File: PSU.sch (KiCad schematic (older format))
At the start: 8 parts

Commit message: created pcb
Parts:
- R5: renamed from R?; footprint Main_LIB:R_0603 -> MAIN_PCB_LIB:R_0603
- gave numbers to parts that had none: 7
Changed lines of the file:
@@
 $Descr A4 11693 8268
 encoding utf-8
-Sheet 2 4
+Sheet 2 5
 Title ""
 Date ""
@@
 	4400 2600 4550 2600
 $Comp
-L Main_Library:C_100nF_0603_50V C?
+L Main_Library:C_100nF_0603_50V C1
 U 1 1 6152505F
 P 3550 2750
-F 0 "C?" H 3628 2796 50  0000 L CNN
+F 0 "C1" H 3628 2796 50  0000 L CNN
 F 1 "C_100nF_0603_50V" H 3500 3100 50  0001 C CNN
 F 2 "MAIN_PCB_LIB:C_0603" H 3500 3100 50  0001 C CNN
@@
 	3550 2600 3800 2600
 $Comp
-L Main_Library:GND #GND?
+L Main_Library:GND #GND04
 U 1 1 61525852
 P 3550 2900
-F 0 "#GND?" H 3390 2880 50  0001 C CNN
+F 0 "#GND04" H 3390 2880 50  0001 C CNN
 F 1 "GND" H 3390 2880 50  0001 C CNN
 F 2 "" H 3460 2840 50  0001 C CNN
@@
 $EndComp
 $Comp
-L Main_Library:R_3K_0603 R?
+L Main_Library:R_3K_0603 R3
 U 1 1 61527697
 P 4550 2800
-F 0 "R?" H 4603 2846 50  0000 L CNN
+F 0 "R3" H 4603 2846 50  0000 L CNN
 F 1 "R_3K_0603" H 4550 2800 50  0001 C CNN
 F 2 "MAIN_PCB_LIB:R_0603" H 4550 2800 50  0001 C CNN
@@
 	4100 3000 4550 3000
 $Comp
-L Main_Library:GND #GND?
+L Main_Library:GND #GND06
 U 1 1 6152B9B3
 P 4250 3200
-F 0 "#GND?" H 4090 3180 50  0001 C CNN
+F 0 "#GND06" H 4090 3180 50  0001 C CNN
 F 1 "GND" H 4090 3180 50  0001 C CNN
 F 2 "" H 4160 3140 50  0001 C CNN
@@
 	4200 3200 4250 3200
 $Comp
-L Main_Library:U_LM317_TH U?
+L Main_Library:U_LM317_TH U1
 U 1 1 61586E8A
 P 4100 2600
-F 0 "U?" H 4100 2775 50  0000 C CNN
+F 0 "U1" H 4100 2775 50  0000 C CNN
 F 1 "U_LM317_TH" H 4100 3000 50  0001 C CNN
 F 2 "MAIN_PCB_LIB:U_LM317_TI_TH" H 4100 3000 50  0001 C CNN
@@
 $EndComp
 $Comp
-L Main_Library:R_10K_Potmeter R?
+L Main_Library:R_10K_Potmeter R2
 U 1 1 615893FF
 P 4100 3200
-F 0 "R?" H 4047 3246 50  0000 R CNN
+F 0 "R2" H 4047 3246 50  0000 R CNN
 F 1 "R_10K_Potmeter" H 4200 3500 50  0001 C CNN
 F 2 "MAIN_PCB_LIB:R_TH_POT_P160series" H 4200 3500 50  0001 C CNN
@@
 	3100 3800 3600 3800
 $Comp
-L Main_Library:C_100nF_0603_50V C?
+L Main_Library:C_100nF_0603_50V C2
 U 1 1 61594EF5
 P 3600 3950
-F 0 "C?" H 3678 3996 50  0000 L CNN
+F 0 "C2" H 3678 3996 50  0000 L CNN
 F 1 "C_100nF_0603_50V" H 3550 4300 50  0001 C CNN
 F 2 "MAIN_PCB_LIB:C_0603" H 3550 4300 50  0001 C CNN
@@
 	3600 3800 3850 3800
 $Comp
-L Main_Library:GND #GND?
+L Main_Library:GND #GND05
 U 1 1 61594EFD
 P 3600 4100
-F 0 "#GND?" H 3440 4080 50  0001 C CNN
+F 0 "#GND05" H 3440 4080 50  0001 C CNN
 F 1 "GND" H 3440 4080 50  0001 C CNN
 F 2 "" H 3510 4040 50  0001 C CNN
@@
 $EndComp
 $Comp
-L Main_Library:R_3K_0603 R?
+L Main_Library:R_3K_0603 R4
 U 1 1 61594F05
 P 4600 4000
-F 0 "R?" H 4653 4046 50  0000 L CNN
+F 0 "R4" H 4653 4046 50  0000 L CNN
 F 1 "R_3K_0603" H 4600 4000 50  0001 C CNN
 F 2 "MAIN_PCB_LIB:R_0603" H 4600 4000 50  0001 C CNN
@@
 	4150 4200 4600 4200
 $Comp
-L Main_Library:U_LM317_TH U?
+L Main_Library:U_LM317_TH U2
 U 1 1 61594F17
 P 4150 3800
-F 0 "U?" H 4150 3975 50  0000 C CNN
+F 0 "U2" H 4150 3975 50  0000 C CNN
 F 1 "U_LM317_TH" H 4150 4200 50  0001 C CNN
 F 2 "MAIN_PCB_LIB:U_LM317_TI_TH" H 4150 4200 50  0001 C CNN
@@
 5V
 $Comp
-L Main_Library:R_9K1_0603 R?
+L Main_Library:R_9K1_0603 R5
 U 1 1 615992A6
 P 4600 4350
-F 0 "R?" H 4653 4388 39  0000 L CNN
+F 0 "R5" H 4653 4388 39  0000 L CNN
 F 1 "R_9K1_0603" H 4550 4900 39  0001 C CNN
-F 2 "Main_LIB:R_0603" H 4600 4850 39  0001 C CNN
+F 2 "MAIN_PCB_LIB:R_0603" H 4600 4850 39  0001 C CNN
 F 3 "" H 4550 4500 39  0001 C CNN
 F 4 "9K1" H 4653 4313 39  0000 L CNN "Waarde"
@@
 Connection ~ 4600 4200
 $Comp
-L Main_Library:GND #GND?
+L Main_Library:GND #GND07
 U 1 1 61599DC1
 P 4600 4500
-F 0 "#GND?" H 4440 4480 50  0001 C CNN
+F 0 "#GND07" H 4440 4480 50  0001 C CNN
 F 1 "GND" H 4440 4480 50  0001 C CNN
 F 2 "" H 4510 4440 50  0001 C CNN

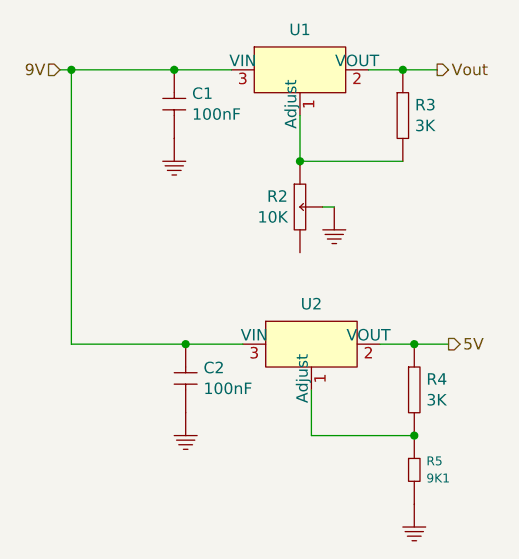
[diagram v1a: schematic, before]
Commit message: added raspberry pi hat pcb outline and layout
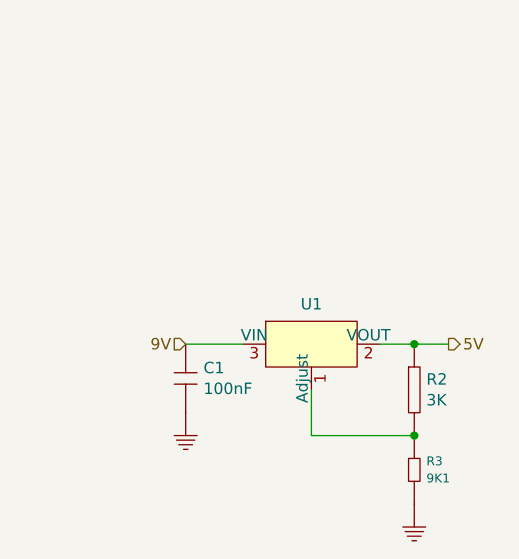
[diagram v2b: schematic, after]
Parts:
- removed C1: C_100nF_0603_50V, MAIN_PCB_LIB:C_0603, symbol Main_Library:C_100nF_0603_50V
- removed R2: R_10K_Potmeter, MAIN_PCB_LIB:R_TH_POT_P160series, symbol Main_Library:R_10K_Potmeter
- removed R3: R_3K_0603, MAIN_PCB_LIB:R_0603, symbol Main_Library:R_3K_0603
- removed U1: U_LM317_TH, MAIN_PCB_LIB:U_LM317_TI_TH, symbol Main_Library:U_LM317_TH
- renumbered C2 to C1, R4 to R2, R5 to R3, U2 to U1
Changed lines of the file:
@@
 Comment4 ""
 $EndDescr
-Text HLabel 3050 2600 0    50   Input ~ 0
+Text HLabel 3600 3800 0    50   Input ~ 0
 9V
-Text HLabel 4700 2600 2    50   Output ~ 0
-Vout
 Wire Wire Line
-	4400 2600 4550 2600
+	4450 3800 4600 3800
 $Comp
 L Main_Library:C_100nF_0603_50V C1
-U 1 1 6152505F
-P 3550 2750
-F 0 "C1" H 3628 2796 50  0000 L CNN
-F 1 "C_100nF_0603_50V" H 3500 3100 50  0001 C CNN
-F 2 "MAIN_PCB_LIB:C_0603" H 3500 3100 50  0001 C CNN
-F 3 "" H 3550 2950 50  0001 C CNN
-F 4 "C105174" H 3500 3050 50  0001 C CNN "LCSC"
-F 5 "100nF" H 3628 2705 50  0000 L CNN "Waarde"
-	1    3550 2750
-	1    0    0    -1
-$EndComp
-Connection ~ 3550 2600
-Wire Wire Line
-	3550 2600 3800 2600
-$Comp
-L Main_Library:GND #GND04
-U 1 1 61525852
-P 3550 2900
-F 0 "#GND04" H 3390 2880 50  0001 C CNN
-F 1 "GND" H 3390 2880 50  0001 C CNN
-F 2 "" H 3460 2840 50  0001 C CNN
-F 3 "" H 3460 2840 50  0001 C CNN
-	1    3550 2900
-	1    0    0    -1
-$EndComp
-$Comp
-L Main_Library:R_3K_0603 R3
-U 1 1 61527697
-P 4550 2800
-F 0 "R3" H 4603 2846 50  0000 L CNN
-F 1 "R_3K_0603" H 4550 2800 50  0001 C CNN
-F 2 "MAIN_PCB_LIB:R_0603" H 4550 2800 50  0001 C CNN
-F 3 "" H 4550 2800 50  0001 C CNN
-F 4 "603-RC0603FR-7W3KL" H 4550 2800 50  0001 C CNN "mouser"
-F 5 "3K" H 4603 2755 50  0000 L CNN "waarde"
-	1    4550 2800
-	1    0    0    -1
-$EndComp
-Connection ~ 4550 2600
-Wire Wire Line
-	4550 2600 4700 2600
-Wire Wire Line
-	4100 3000 4100 2800
-Wire Wire Line
-	4100 3000 4550 3000
-$Comp
-L Main_Library:GND #GND06
-U 1 1 6152B9B3
-P 4250 3200
-F 0 "#GND06" H 4090 3180 50  0001 C CNN
-F 1 "GND" H 4090 3180 50  0001 C CNN
-F 2 "" H 4160 3140 50  0001 C CNN
-F 3 "" H 4160 3140 50  0001 C CNN
-	1    4250 3200
-	1    0    0    -1
-$EndComp
-Wire Wire Line
-	4200 3200 4250 3200
-$Comp
-L Main_Library:U_LM317_TH U1
-U 1 1 61586E8A
-P 4100 2600
-F 0 "U1" H 4100 2775 50  0000 C CNN
-F 1 "U_LM317_TH" H 4100 3000 50  0001 C CNN
-F 2 "MAIN_PCB_LIB:U_LM317_TI_TH" H 4100 3000 50  0001 C CNN
-F 3 "" H 4100 3000 50  0001 C CNN
-F 4 "863-LM317TG" H 4100 2600 50  0001 C CNN "Mouser"
-	1    4100 2600
-	1    0    0    -1
-$EndComp
-$Comp
-L Main_Library:R_10K_Potmeter R2
-U 1 1 615893FF
-P 4100 3200
-F 0 "R2" H 4047 3246 50  0000 R CNN
-F 1 "R_10K_Potmeter" H 4200 3500 50  0001 C CNN
-F 2 "MAIN_PCB_LIB:R_TH_POT_P160series" H 4200 3500 50  0001 C CNN
-F 3 "" H 4200 3500 50  0001 C CNN
-F 4 "10K" H 4047 3155 50  0000 R CNN "Waarde"
-	1    4100 3200
-	1    0    0    -1
-$EndComp
-Connection ~ 4100 3000
-Wire Wire Line
-	4450 3800 4600 3800
-Wire Wire Line
-	3100 3800 3600 3800
-$Comp
-L Main_Library:C_100nF_0603_50V C2
 U 1 1 61594EF5
 P 3600 3950
-F 0 "C2" H 3678 3996 50  0000 L CNN
+F 0 "C1" H 3678 3996 50  0000 L CNN
 F 1 "C_100nF_0603_50V" H 3550 4300 50  0001 C CNN
 F 2 "MAIN_PCB_LIB:C_0603" H 3550 4300 50  0001 C CNN
@@
 	1    0    0    -1
 $EndComp
-Connection ~ 3600 3800
 Wire Wire Line
 	3600 3800 3850 3800
 $Comp
-L Main_Library:GND #GND05
+L Main_Library:GND #GND04
 U 1 1 61594EFD
 P 3600 4100
-F 0 "#GND05" H 3440 4080 50  0001 C CNN
+F 0 "#GND04" H 3440 4080 50  0001 C CNN
 F 1 "GND" H 3440 4080 50  0001 C CNN
 F 2 "" H 3510 4040 50  0001 C CNN
@@
 $EndComp
 $Comp
-L Main_Library:R_3K_0603 R4
+L Main_Library:R_3K_0603 R2
 U 1 1 61594F05
 P 4600 4000
-F 0 "R4" H 4653 4046 50  0000 L CNN
+F 0 "R2" H 4653 4046 50  0000 L CNN
 F 1 "R_3K_0603" H 4600 4000 50  0001 C CNN
 F 2 "MAIN_PCB_LIB:R_0603" H 4600 4000 50  0001 C CNN
@@
 	4150 4200 4600 4200
 $Comp
-L Main_Library:U_LM317_TH U2
+L Main_Library:U_LM317_TH U1
 U 1 1 61594F17
 P 4150 3800
-F 0 "U2" H 4150 3975 50  0000 C CNN
+F 0 "U1" H 4150 3975 50  0000 C CNN
 F 1 "U_LM317_TH" H 4150 4200 50  0001 C CNN
 F 2 "MAIN_PCB_LIB:U_LM317_TI_TH" H 4150 4200 50  0001 C CNN
@@
 	1    0    0    -1
 $EndComp
-Wire Wire Line
-	3100 3800 3100 2600
-Wire Wire Line
-	3050 2600 3100 2600
-Connection ~ 3100 2600
-Wire Wire Line
-	3100 2600 3550 2600
 Text HLabel 4750 3800 2    50   Output ~ 0
 5V
 $Comp
-L Main_Library:R_9K1_0603 R5
+L Main_Library:R_9K1_0603 R3
 U 1 1 615992A6
 P 4600 4350
-F 0 "R5" H 4653 4388 39  0000 L CNN
+F 0 "R3" H 4653 4388 39  0000 L CNN
 F 1 "R_9K1_0603" H 4550 4900 39  0001 C CNN
 F 2 "MAIN_PCB_LIB:R_0603" H 4600 4850 39  0001 C CNN
@@
 Connection ~ 4600 4200
 $Comp
-L Main_Library:GND #GND07
+L Main_Library:GND #GND05
 U 1 1 61599DC1
 P 4600 4500
-F 0 "#GND07" H 4440 4480 50  0001 C CNN
+F 0 "#GND05" H 4440 4480 50  0001 C CNN
 F 1 "GND" H 4440 4480 50  0001 C CNN
 F 2 "" H 4510 4440 50  0001 C CNN
